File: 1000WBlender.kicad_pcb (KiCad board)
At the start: 2 copper layers, 19 parts, among them J1 Conn_01x02_Female, J2 Conn_01x02_Female, J3 Conn_01x02_Female, J4 Conn_01x02_Female, SW1 SW_DPDT_x2, U1 TL072

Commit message: work on pcb design
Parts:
- removed D1: LED, LED_THT:LED_D5.0mm-3
- removed R4: 330, Resistor_SMD:R_0805_2012Metric_Pad1.15x1.40mm_HandSolder
- removed RV2: 1M, Potentiometer_THT:Potentiometer_Omeg_PC16BU_Vertical
- removed SW1: SW_DPDT_x2, Connector_PinHeader_2.54mm:PinHeader_2x06_P2.54mm_Vertical
- moved C4 63.1 mm to (156.0, 131.8)
- moved C3 61.4 mm to (143.8, 131.8)
- moved J2 58.2 mm to (138.4, 128.3)
- moved C1 58.1 mm to (149.9, 143.0), turned to 270 degrees
- moved J1 56.5 mm to (138.4, 133.3)
- moved J3 53.7 mm to (161.3, 128.3)
- moved BT1 52.9 mm to (161.3, 143.5)
- moved RV1 51.7 mm to (154.9, 127.0), turned to 270 degrees
- moved R5 50.7 mm to (143.8, 145.8), turned to 0 degrees
- moved J4 50.4 mm to (161.3, 133.3)
- moved R6 47.7 mm to (143.8, 138.9)
- moved U1 47.4 mm to (149.9, 133.9)
- moved R2 43.6 mm to (143.8, 142.2), turned to 180 degrees
- moved C2 43.1 mm to (143.8, 135.9)
- moved R1 40.4 mm to (138.7, 136.7)
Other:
- board outline added: 27.4 x 23.4 mm
- rule trace_min: 0.2 -> 0.1524
- rule via_min_drill: 0.3 -> 0.3302
- rule via_min_size: 0.4 -> 0.6858

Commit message: routing done, gerbers exported, rev2 complete
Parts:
- removed J1: Conn_01x02_Female, Connector_PinHeader_2.54mm:PinHeader_1x01_P2.54mm_Vertical
- added G***: LOGO, Symbol:nayong, B.Cu at (150.1, 136.9)
- added IN: Conn_01x02_Female, Connector_PinHeader_2.54mm:PinHeader_1x01_P2.54mm_Vertical, F.Cu at (138.4, 133.3)
- added REF**: TestPoint_Bridge_Pitch2.54mm_Drill1.0mm, TestPoint:TestPoint_Bridge_Pitch2.54mm_Drill1.0mm, F.Cu at (138.2, 145.8)
- U1: footprint Package_SO:SOIC-8-1EP_3.9x4.9mm_P1.27mm_EP2.29x3mm -> Package_SO:SO-8_3.9x4.9mm_P1.27mm
- moved R1 0.80 mm to (138.4, 137.4), turned to 270 degrees
- turned C4 to 180 degrees
- renumbered BT1 to +9V, J4 to OUT, J3 to RTRN, J2 to SEND
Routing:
- net +9V: track 0.00 -> 28.4 mm
- net GND: track 0.00 -> 26.6 mm
- net OUT: track 0.00 -> 14.9 mm
- net Net-(C2-Pad1): track 0.00 -> 14.8 mm
- net Net-(C4-Pad1): track 0.00 -> 14.0 mm
- net Net-(C4-Pad2): track 0.00 -> 9.11 mm
- net IN: track 0.00 -> 7.26 mm
- net RTRN: track 0.00 -> 6.88 mm
- net +4.5V: track 0.00 -> 6.86 mm
- net SEND: track 0.00 -> 6.65 mm
- net Net-(C3-Pad2): track 0.00 -> 3.82 mm
- added copper zone on B.Cu, net GND
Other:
- net class Default: clearance 0.2 -> 0.254; trace_width 0.25 -> 0.635; via_dia 0.8 -> 0.762; via_drill 0.4 -> 0.635
- net class Minimal added: clearance 0.0508, trace_width 0.1524, via_dia 0.6858, via_drill 0.635
- rule trace_clearance: 0.2 -> 0.254
- board text added: "1000W Blender"

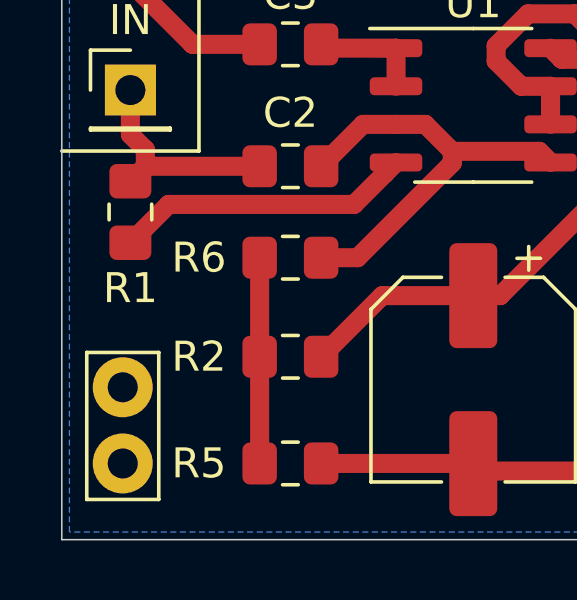
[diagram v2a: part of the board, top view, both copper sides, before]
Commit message: fixing kicad_pcb file to work with kicad 5.1 as opposed to nightly
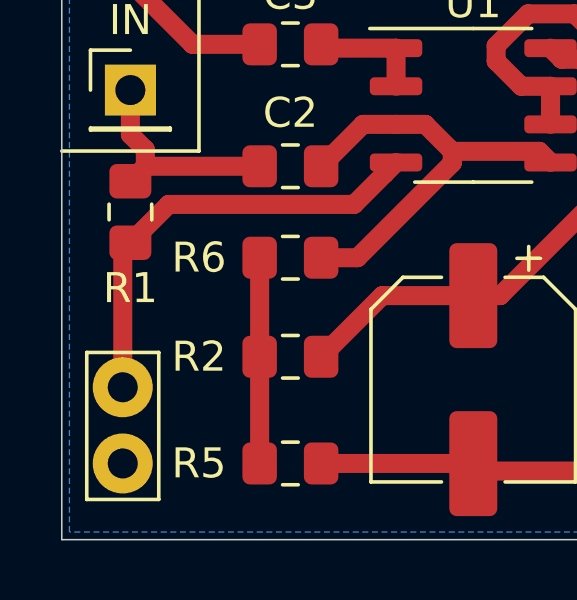
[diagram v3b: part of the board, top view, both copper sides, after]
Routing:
- net GND: track 26.6 -> 31.5 mm
